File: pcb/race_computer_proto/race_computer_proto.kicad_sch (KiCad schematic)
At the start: 13 parts, among them U1 Teensy4.0, U3 SN74LVC245APW, U8 74LS125

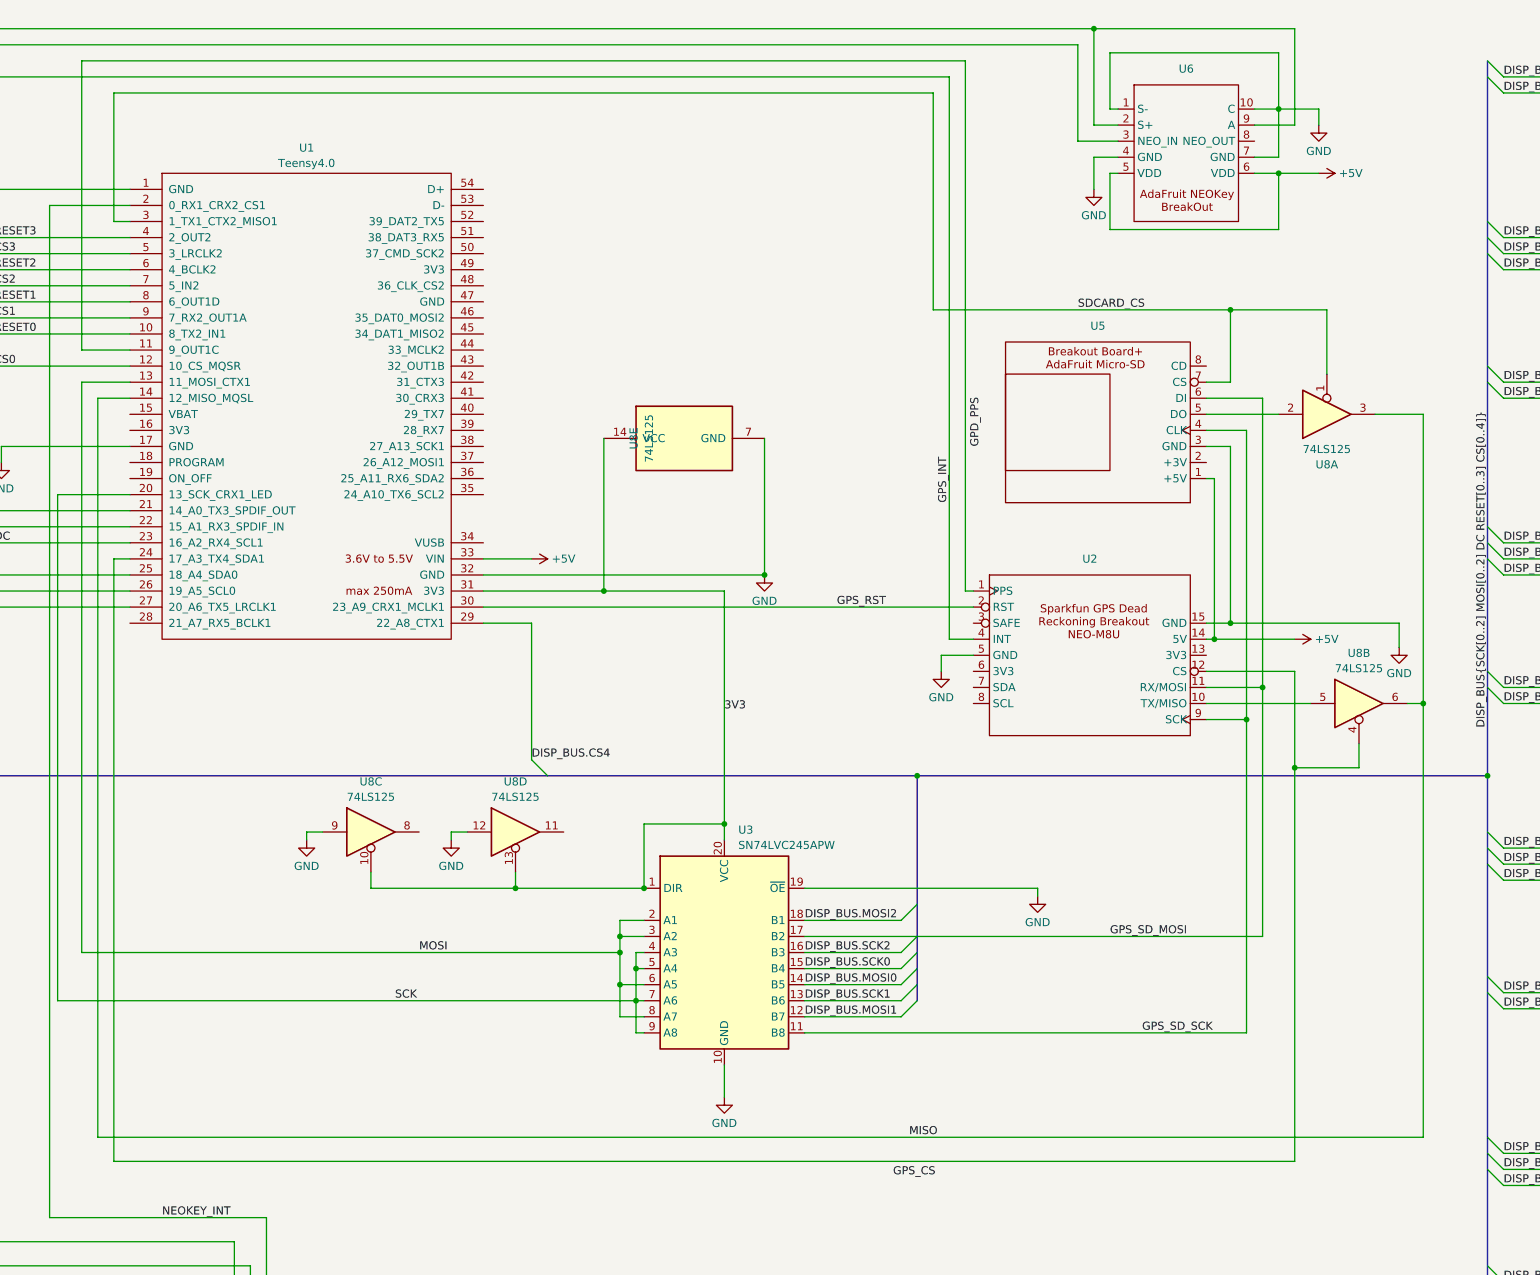
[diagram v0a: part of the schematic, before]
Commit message: Update PCB to account for second SPI connection -- note that the initial routing was just thrown together and needs to be reviewed and cleaned up.
Remove doSPILock()/doSPIUnlock() calls from storage code as they are not needed anymore.

Add timezone definitions and a timeDateSettings class to handle the timezone.  Still need to add menu to configure timezone.
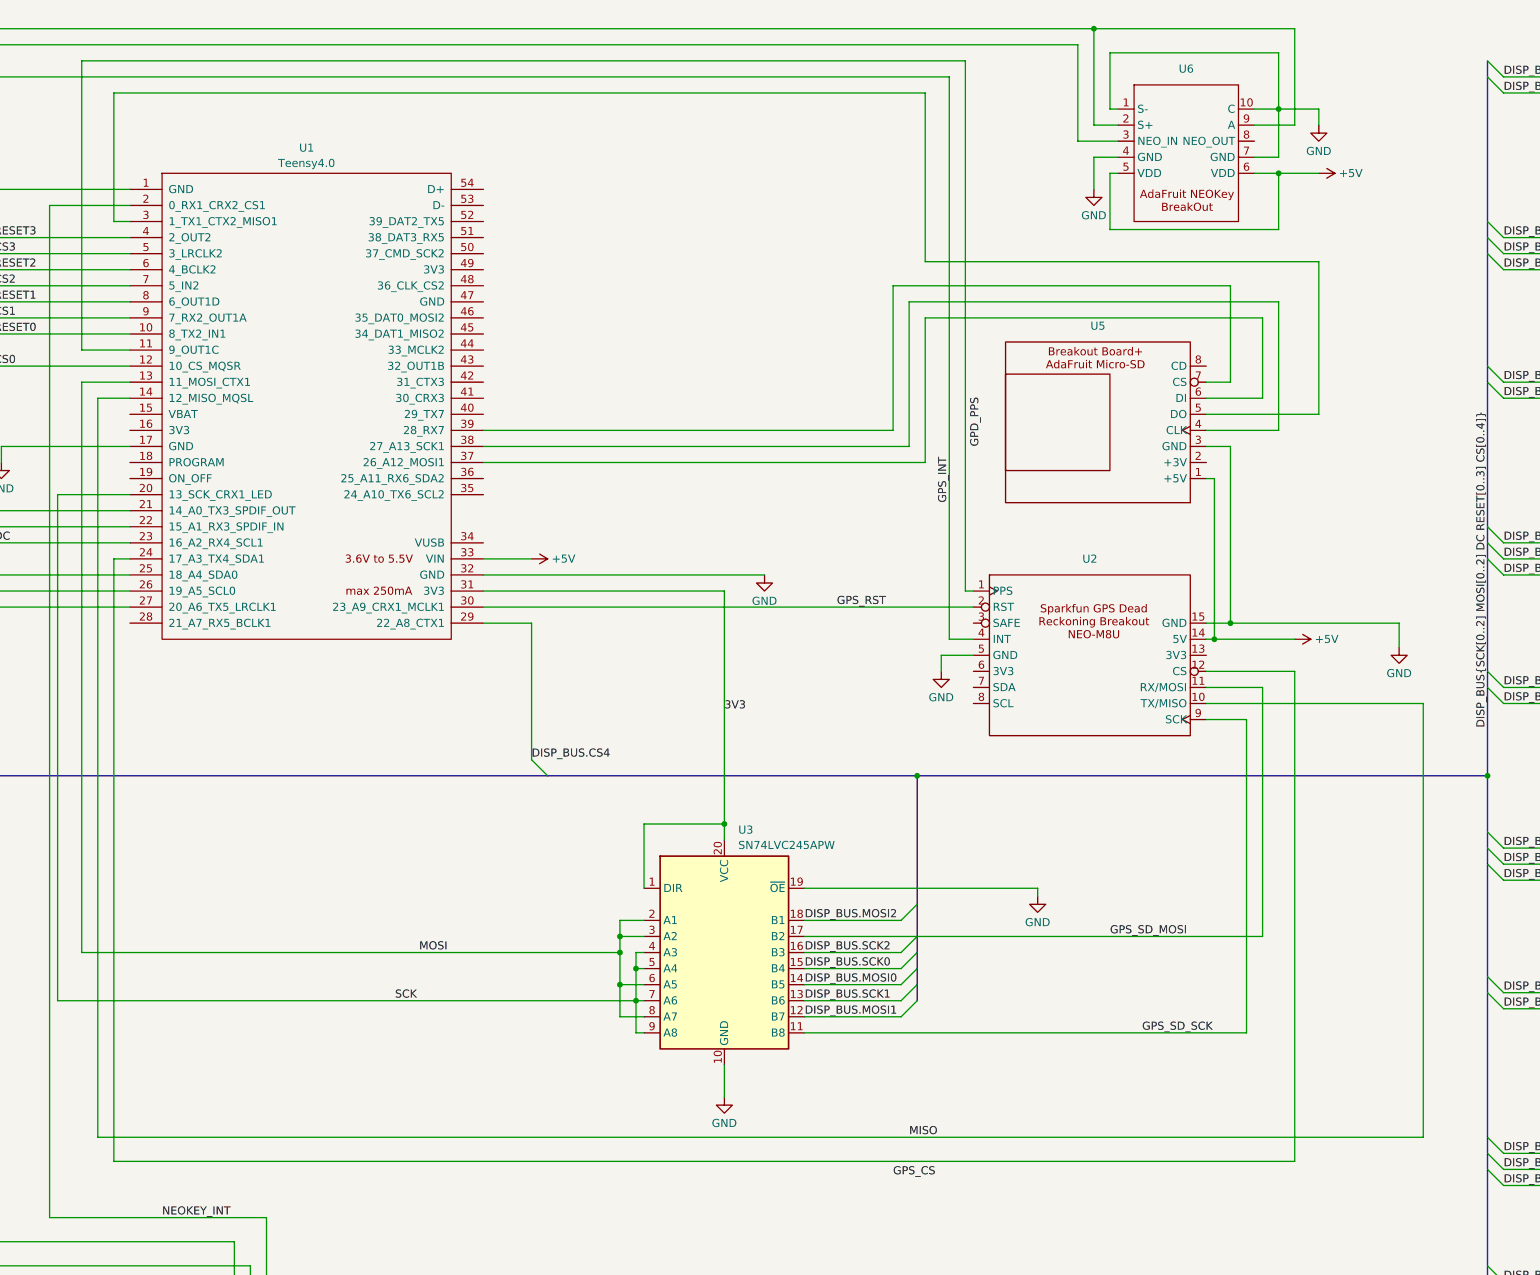
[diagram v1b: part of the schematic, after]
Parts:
- removed U8: 74LS125, Package_DIP:DIP-14_W7.62mm_Socket_LongPads, symbol 74xx:74LS125
- U1: footprint race_computer:teensy4_0_reduced -> race_computer:Teensy40_reduced1
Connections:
- net GPS_SD_MOSI: no longer U5.6 (DI)
- net GPS_SD_SCK: no longer U5.4 (CLK)
- net MISO: now also U2.10 (TX/MISO)
- net at U1.37 (26_A12_MOSI1): now also U5.6 (DI)
- net at U1.38 (27_A13_SCK1): now also U5.4 (CLK)
- net at U1.39 (28_RX7): now also U5.7 (CS)
- net at U5.5 (DO): now also U1.3 (1_TX1_CTX2_MISO1)
- removed net SDCARD_CS: U1.3 (1_TX1_CTX2_MISO1), U5.7 (CS)

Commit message: Fairly substantial change set that brings in PCB changes from re-routing the board supporting a second SPI port dedicated to the SD card.  Still needs review and testing of all the new pin assignments to ensure everything supports what has been assigned to it -- not all pins can be used for all counters, etc.  Also begins a bunch of code cleanup.  The code was thrown together in a "it works, move on" paradigm, with some thought to the future, but not a lot.  This starts the clean up to make things more supportable long term, and hopefully easier to add features to.  The fixes here are minor, but a start.
Removed the original test code that started the whole project.  It was a mash of library
examples and thrown together code that wouldn't run on anything.

Added a GPS synced clock -- very very simple.  Used the same GPS module and LED display.
It has enough functionality to ensure that the race computer was starting in sync with
GPS time when in delayed start mode.  It is.  Will leave the code here though as it may
be useful in the future.

More details updates and fixes follow.

pcb: update race computer prototype to revision 3.0

- Bump PCB revision from 2.2 to 3.0

- Add J3 (2-pin JST XH) wheel speed sensor input connector and optocoupler
  isolation from microcontroller.  Wheel speed input is designed to be driven
  for an open collector driver.

- Add J1 (3-pin JST XH) I2C communication breakout connector.  Options for future
  expansion.

- Add J2 (3-pin JST XH) serial communication breakout connector.  Options for
  future expandsion

- Reposition headers

- Reorganize net assignments throughout the board to simplify routing.  Will
  require code updates when switching to new board.  Need to confirm all pins
  support their expected functionality.

refactor: encapsulate OLED displays into display_t objects

- Introduce display class that wraps U8G2 display objects, each
  managing its own content list instead of a single global list

- Replace raw buffer poin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
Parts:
- added J1: I2C_Comm, Connector_JST:JST_XH_B3B-XH-A_1x03_P2.50mm_Vertical, symbol Connector_Generic:Conn_01x03
- added J2: Serial_Comm, Connector_JST:JST_XH_B3B-XH-A_1x03_P2.50mm_Vertical, symbol Connector_Generic:Conn_01x03
- added J3: Wheel_Speed, Connector_JST:JST_XH_B2B-XH-A_1x02_P2.50mm_Vertical, symbol Connector_Generic:Conn_01x02
- added R1: 10K, Resistor_THT:R_Axial_DIN0204_L3.6mm_D1.6mm_P5.08mm_Horizontal, symbol Device:R_US
- added R2: 1K, Resistor_THT:R_Axial_DIN0204_L3.6mm_D1.6mm_P5.08mm_Horizontal, symbol Device:R_US
- added U8: EL817, Package_DIP:DIP-4_W7.62mm, symbol Isolator:EL817
- U5: footprint race_computer:microsd_breakout_header -> Connector_JST:JST_XH_B8B-XH-A_1x08_P2.50mm_Vertical
- U6: footprint race_computer:neokey_header -> Connector_JST:JST_XH_B5B-XH-AM_1x05_P2.50mm_Vertical
- U7: footprint race_computer:neokey_1x4_header -> Connector_JST:JST_XH_B6B-XH-A_1x06_P2.50mm_Vertical
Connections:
- net +5V: now also R2.1; no longer U6.6 (VDD)
- net 3V3: now also R1.2
- net DISP_BUS.CS0: now also U1.10 (8_TX2_IN1); no longer U1.12 (10_CS_MQSR)
- net DISP_BUS.CS1: now also U1.8 (6_OUT1D); no longer U1.9 (7_RX2_OUT1A)
- net DISP_BUS.CS2: now also U1.6 (4_BCLK2); no longer U1.7 (5_IN2)
- net DISP_BUS.CS3: now also U1.4 (2_OUT2); no longer U1.5 (3_LRCLK2)
- net DISP_BUS.DC: now also U1.43 (32_OUT1B); no longer U1.23 (16_A2_RX4_SCL1)
- net DISP_BUS.RESET0: now also U1.12 (10_CS_MQSR); no longer U1.10 (8_TX2_IN1)
- net DISP_BUS.RESET1: now also U1.9 (7_RX2_OUT1A); no longer U1.8 (6_OUT1D)
- net DISP_BUS.RESET2: now also U1.7 (5_IN2); no longer U1.6 (4_BCLK2)
- net DISP_BUS.RESET3: now also U1.5 (3_LRCLK2); no longer U1.4 (2_OUT2)
- net GND: now also J1.3 (Pin_3), J2.3 (Pin_3), J3.2 (Pin_2), U8.3; no longer U6.10 (C), U6.7 (GND)
- net GPS_CS: now also U1.2 (0_RX1_CRX2_CS1), U2.12 (CS)
- net NEOKEY_INT: now also U1.28 (21_A7_RX5_BCLK1); no longer U1.2 (0_RX1_CRX2_CS1)
- net at U1.21 (14_A0_TX3_SPDIF_OUT): now also R1.1, U8.4; no longer U6.3 (NEO_IN)
- net at U1.22 (15_A1_RX3_SPDIF_IN), U6.2 (S+): no longer U6.9 (A)
- net at U1.24 (17_A3_TX4_SDA1): now also J2.1 (Pin_1); no longer U2.12 (CS)
- net at U1.35 (24_A10_TX6_SCL2): now also J1.2 (Pin_2)
- net at U1.36 (25_A11_RX6_SDA2): now also J1.1 (Pin_1)
- net at U1.39 (28_RX7): no longer U5.7 (CS)
- net at U1.41 (30_CRX3): now also U5.7 (CS)
- net at U1.42 (31_CTX3): now also U6.3 (NEO_IN)
- new net: J2.2 (Pin_2), U1.23 (16_A2_RX4_SCL1)
- new net: R2.2, U8.1
- new net: J3.1 (Pin_1), U8.2
